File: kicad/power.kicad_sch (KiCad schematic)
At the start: 28 parts, among them J1 L, J10 PE, J2 N, J7 PE, J8 PE, J9 PE, Q5 BD677, U3 LM317

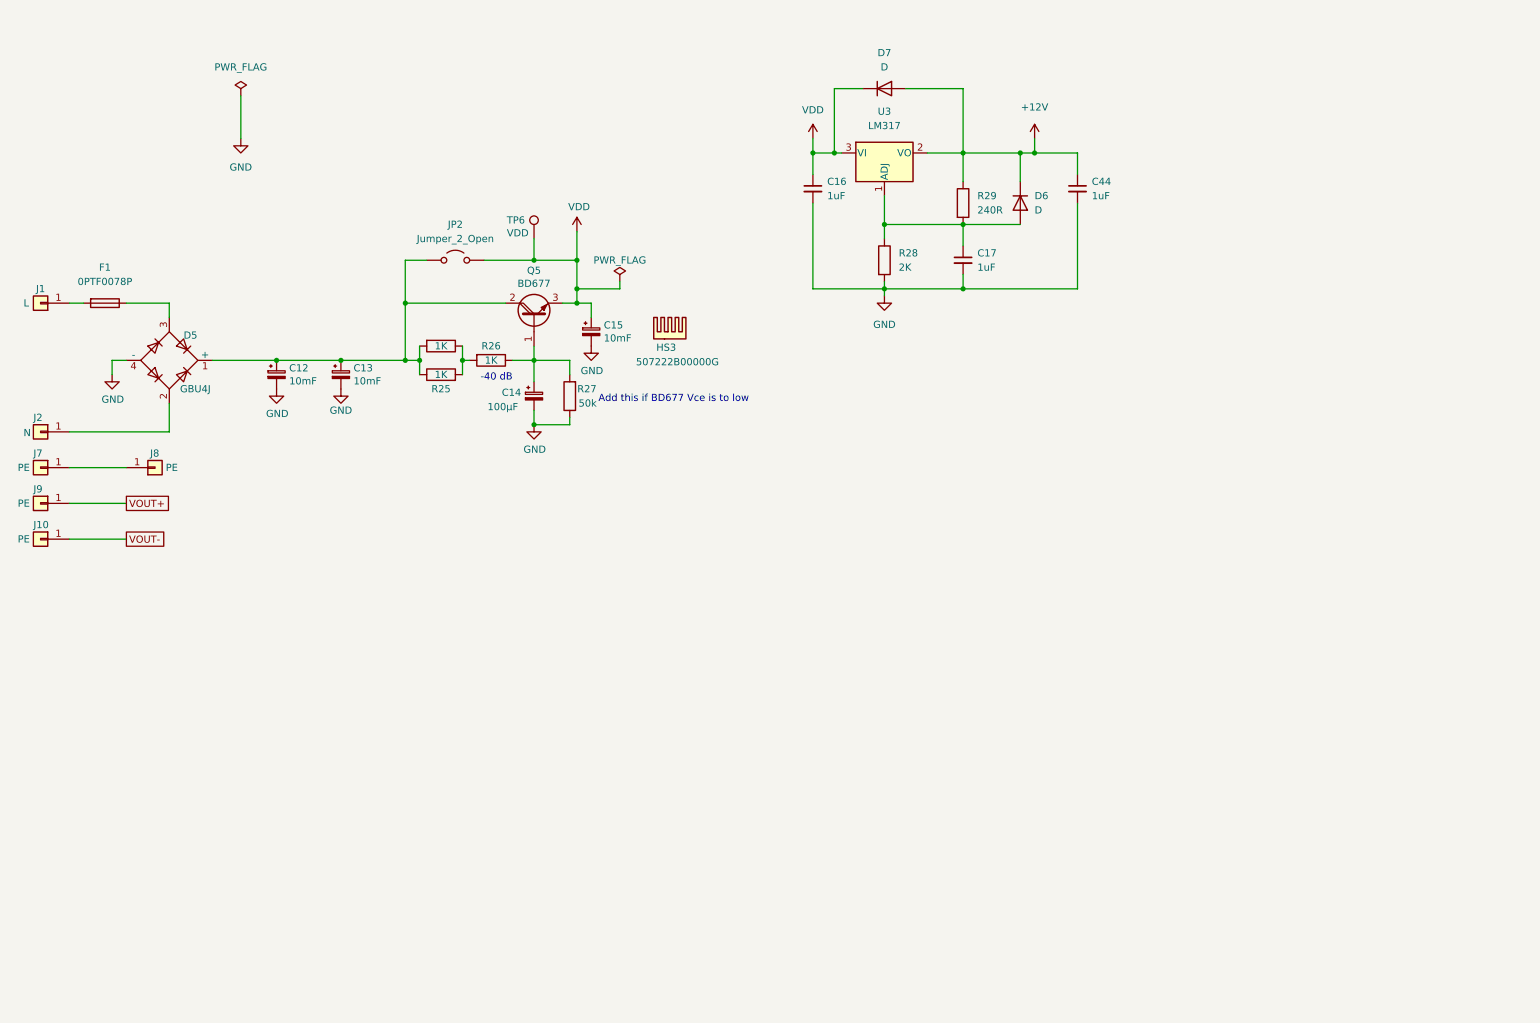
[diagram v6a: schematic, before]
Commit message: Changes and added Buck converter for 3V3
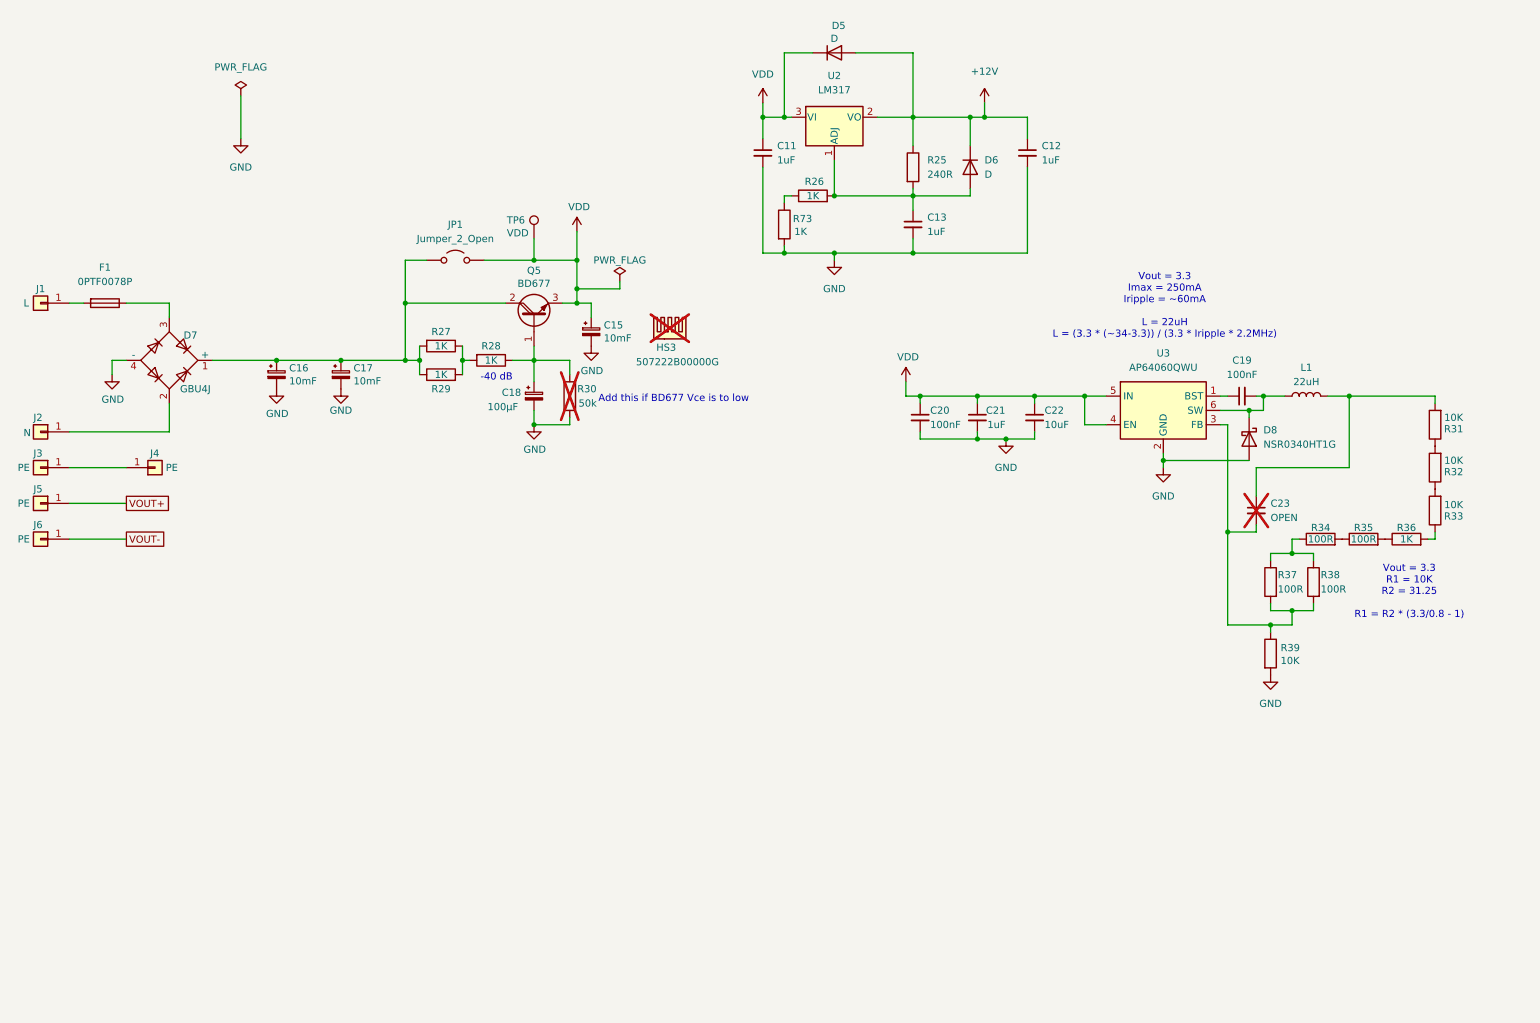
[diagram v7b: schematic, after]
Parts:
- added C19, C20: 100nF, Capacitor_SMD:C_0805_2012Metric_Pad1.18x1.45mm_HandSolder, symbol Device:C_Small
- added C21: 1uF, Capacitor_SMD:C_0805_2012Metric_Pad1.18x1.45mm_HandSolder, symbol Device:C_Small
- added C22: 10uF, Capacitor_SMD:C_1206_3216Metric_Pad1.33x1.80mm_HandSolder, symbol Device:C_Small
- added C23: OPEN, Capacitor_SMD:C_0805_2012Metric_Pad1.18x1.45mm_HandSolder, symbol Device:C_Small
- added D8: NSR0340HT1G, Diode_SMD:D_SOD-323_HandSoldering, symbol Device:D_Schottky
- added L1: 22uH, Inductor_SMD:L_Coilcraft_MSS1246-XXX, symbol Device:L
- added R31, R32, R33, R39: 10K, Resistor_SMD:R_0805_2012Metric_Pad1.20x1.40mm_HandSolder, symbol Device:R
- added R34, R35, R37, R38: 100R, Resistor_SMD:R_0805_2012Metric_Pad1.20x1.40mm_HandSolder, symbol Device:R
- added R36, R73: 1K, Resistor_SMD:R_0805_2012Metric_Pad1.20x1.40mm_HandSolder, symbol Device:R
- added U3: AP64060QWU, Package_TO_SOT_SMD:TSOT-23-6, symbol symbols:AP64060QWU
- C11: renamed from C16; MPN (none) -> CL21B105KBFNNNF
- C12: renamed from C44; MPN (none) -> CL21B105KBFNNNF
- C13: renamed from C17; MPN (none) -> CL21B105KBFNNNF
- C18: renamed from C14; MPN (none) -> EKZN500ELL101MHB5D
- D7: renamed from D5; MPN (none) -> GBU4J
- F1: MPN (none) -> 0PTF0078P
- HS3: now not fitted
- Q5: MPN (none) -> BD677
- R26: renamed from R28; value 2K -> 1K
- R30: renamed from R27; now not fitted
- TP6: footprint TestPoint:TestPoint_Pad_D1.0mm -> TestPoint:TestPoint_Pad_D1.5mm
- U2: renamed from U3; MPN (none) -> LM317
- renumbered C12 to C16, C13 to C17, D7 to D5, J7 to J3, J8 to J4, J9 to J5, J10 to J6, JP2 to JP1, R29 to R25, R24 to R27, R26 to R28, R25 to R29
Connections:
- net GND: now also C20.2, C21.2, C22.2, D8.2 (A), R39.2, R73.2, U3.2 (GND); no longer R26.2
- net VDD: now also C20.1, C21.1, C22.1, U3.4 (EN), U3.5 (IN)
- net at C13.1, D6.2 (A), R25.2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: now also R26.2; no longer R26.1
- new net: R34.1, R37.1, R38.1
- new net: C23.2, R37.2, R38.2, R39.1, U3.3 (FB)
- new net: C23.1, L1.2, R31.2
- new net: R26.1, R73.1
- new net: R34.2, R35.1
- new net: R31.1, R32.2
- new net: R32.1, R33.2
- new net: C19.1, U3.1 (BST)
- new net: C19.2, D8.1 (K), L1.1, U3.6 (SW)
- new net: R33.1, R36.2
- new net: R35.2, R36.1
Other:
- note added: "Vout = 3.3 Imax = 250mA Iripple = ~60mA L = 22uH L = (3.3 * (~34-3.3)) / (3.3 * Iripple * 2.2MHz)"
- note added: "Vout = 3.3 R1 = 10K R2 = 31.25 R1 = R2 * (3.3/0.8 - 1)"
- moved on the sheet: C11, C12, C13, D5, D6, R25, R26, U2

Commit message: Changes
- USB C connector
- 12V Buck converter instead of LM317
- Bunch of stuff I don't remember
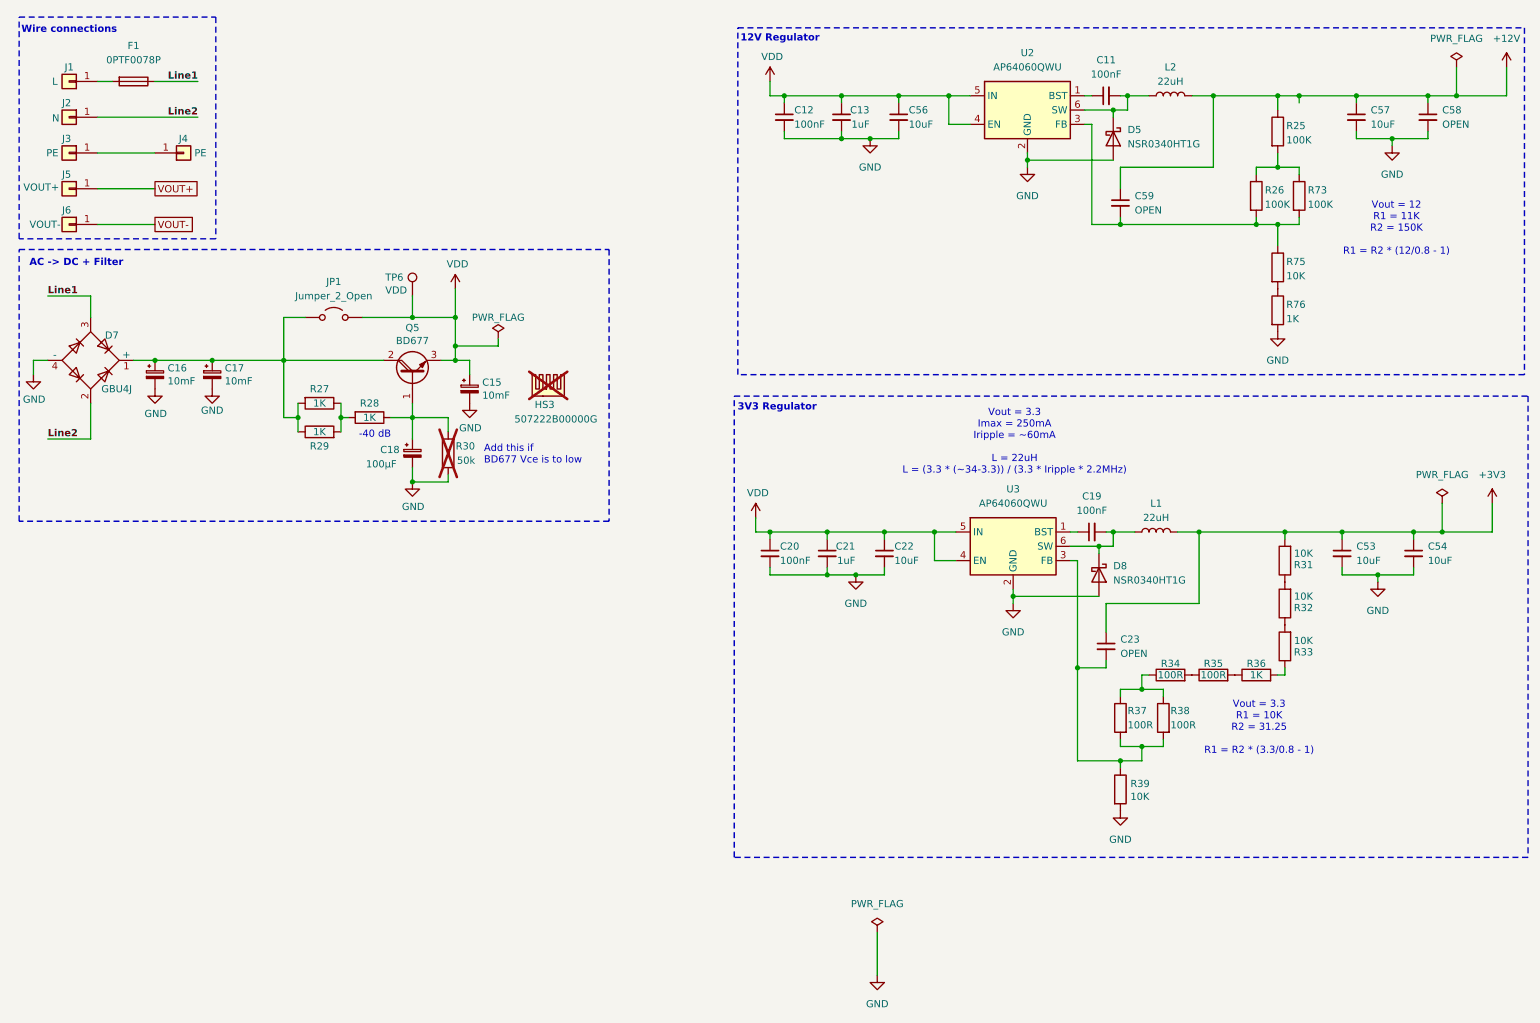
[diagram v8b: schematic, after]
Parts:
- removed D5, D6: D, Diode_SMD:D_SMA_Handsoldering, symbol Device:D
- removed U2: LM317, Package_TO_SOT_THT:TO-220-3_Vertical, symbol Regulator_Linear:LM317_TO-220
- added C53, C54, C57: 10uF, Capacitor_SMD:C_0805_2012Metric_Pad1.18x1.45mm_HandSolder, symbol Device:C_Small
- added C56: 10uF, Capacitor_SMD:C_1206_3216Metric_Pad1.33x1.80mm_HandSolder, symbol Device:C_Small
- added C58, C59: OPEN, Capacitor_SMD:C_0805_2012Metric_Pad1.18x1.45mm_HandSolder, symbol Device:C_Small
- added D5: NSR0340HT1G, Diode_SMD:D_SOD-323_HandSoldering, symbol Device:D_Schottky
- added L2: 22uH, Inductor_SMD:L_Coilcraft_MSS1246-XXX, symbol Device:L
- added R75: 10K, Resistor_SMD:R_0805_2012Metric_Pad1.20x1.40mm_HandSolder, symbol Device:R
- added R76: 1K, Resistor_SMD:R_0805_2012Metric_Pad1.20x1.40mm_HandSolder, symbol Device:R
- added U2: AP64060QWU, Package_TO_SOT_SMD:TSOT-23-6, symbol symbols:AP64060QWU
- C11, C12: value 1uF -> 100nF; MPN CL21B105KBFNNNF -> CC0805KRX7R9BB104
- C23: now fitted
- J5: value PE -> VOUT+
- J6: value PE -> VOUT-
- R25: value 240R -> 100K; MPN (none) -> CRCW080510K0FKEAC
- R26, R73: value 1K -> 100K; MPN (none) -> CRCW080510K0FKEAC
- R27, R28, R29, R36: MPN (none) -> RC0805FR-131KL
- R31, R32, R33, R39: MPN RC0805FR-1310KL -> RC0805FR-1310KL
- R34, R35, R37, R38: MPN (none) -> RC0805FR-13100RL
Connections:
- net +12V: now also C57.1, C58.1, C59.1, L2.2; no longer C12.1
- net GND: now also C53.2, C54.2, C56.2, C57.2, C58.2, D5.2 (A), R76.2, U2.2 (GND); no longer C11.2, R73.2
- net VDD: now also C12.1, C13.1, C56.1, U2.4 (EN), U2.5 (IN); no longer C11.1
- net Line2: now reaches D7.2, J2.1 (Pin_1)
- net Line1: now reaches D7.3, F1.1
- net +3V3: now reaches C23.1, L1.2, R31.2
- net +3V3: now also C53.1, C54.1
- net at R26.1, R73.1: now also R25.2
- new net: C59.2, R26.2, R73.2, R75.1, U2.3 (FB)
- new net: C11.1, U2.1 (BST)
- new net: C11.2, D5.1 (K), L2.1, U2.6 (SW)
- new net: R75.2, R76.1
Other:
- note added: "12V Regulator"
- note added: "3V3 Regulator"
- note added: "AC -> DC + Filter"
- note added: "Vout = 12 R1 = 11K R2 = 150K R1 = R2 * (12/0.8 - 1)"
- note added: "Wire connections"
- moved on the sheet: C15, C16, C17, C18, C19, C20, C21, C22, D7, D8, F1, HS3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
